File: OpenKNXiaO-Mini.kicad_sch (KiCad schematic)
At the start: 8 parts, among them J1 Conn_KNX, J5 Conn_01x05, J7 Conn_01x12, SW1 Prog BTN, U1 Seeeduino XIAO

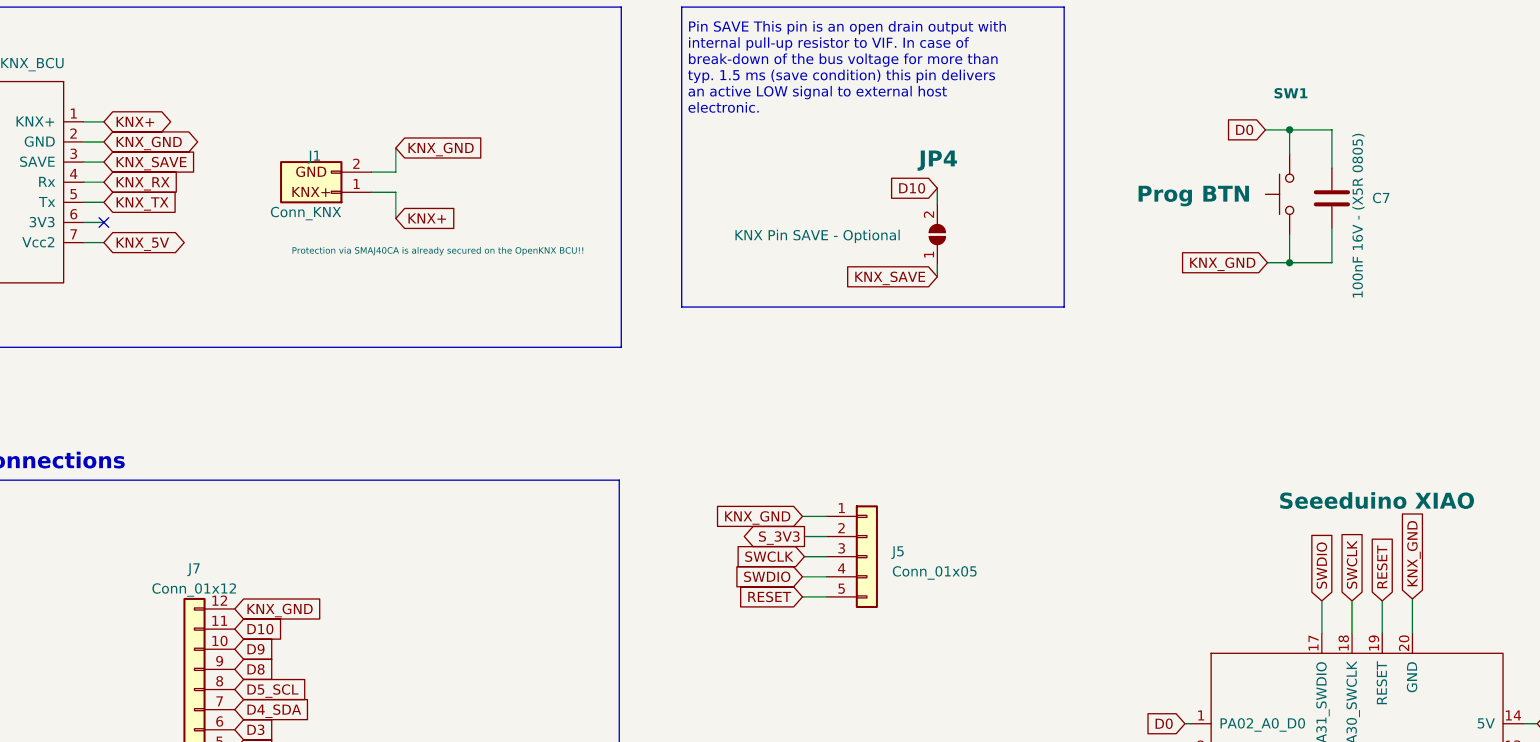
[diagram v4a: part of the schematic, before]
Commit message: Pre-Final
ToDo - Move Save <--> D10 bridge to a reachable place on the pcb
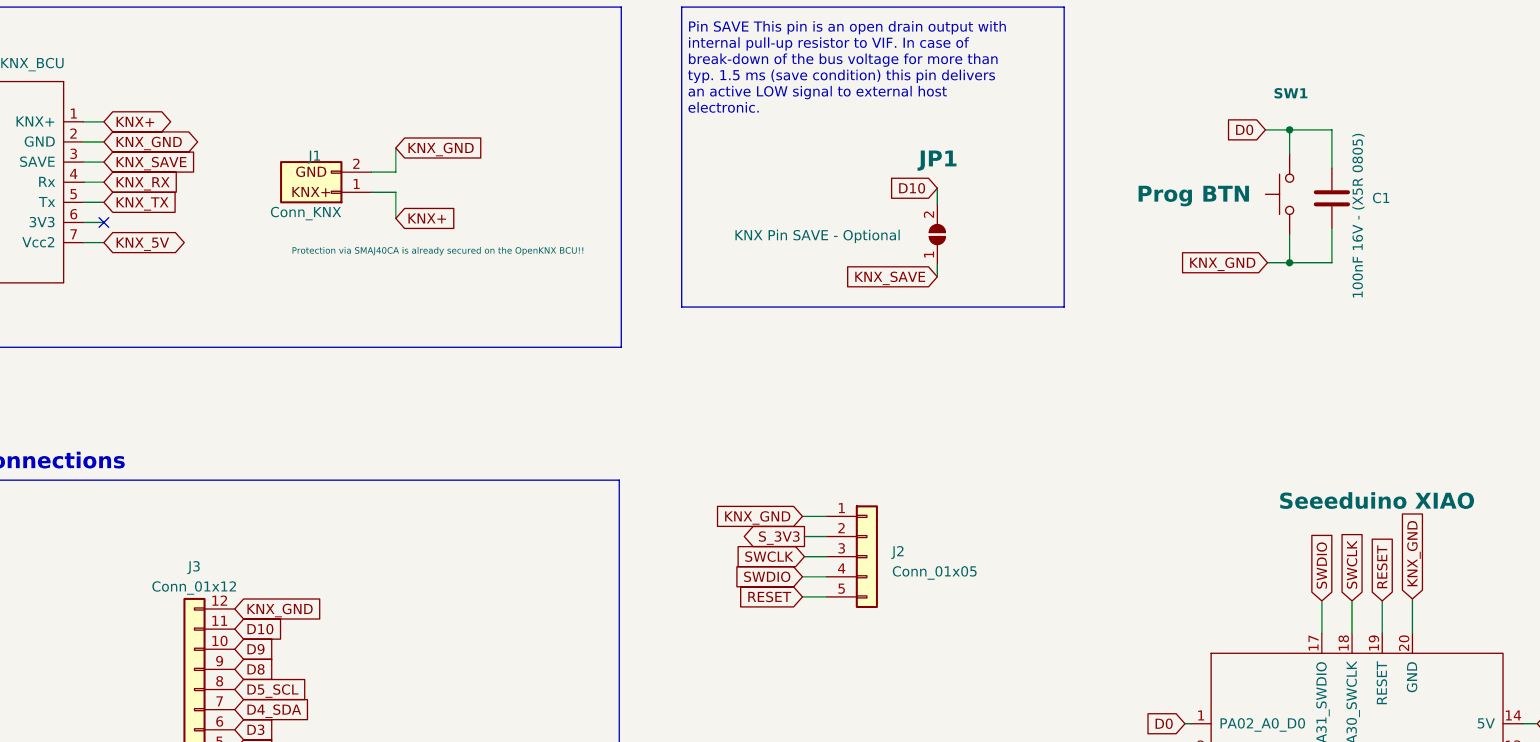
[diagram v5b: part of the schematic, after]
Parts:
- J2: renamed from J5; footprint Connector_JST:JST_SHL_SM05B-SHLS-TF_1x05-1MP_P1.00mm_Horizontal -> Connector_PinHeader_1.00mm:PinHeader_1x05_P1.00mm_Vertical
- renumbered C7 to C1, J7 to J3, JP4 to JP1
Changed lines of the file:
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@@
   (symbol (lib_id "KNeoPix.symbols:SolderJumper_2_Open") (at 142.494 52.07 90) (unit 1)
     (in_bom yes) (on_board yes) (dnp no)
-    (property "Reference" "JP4" (at 142.621 42.545 90)
+    (property "Reference" "JP1" (at 142.621 42.545 90)
       (effects (font (size 2 2) bold))
     )
@@
       (project "OpenKNXiaO-Mini"
         (path "/e63e39d7-6ac0-4ffd-8aa3-1841a4541b55"
-          (reference "JP4") (unit 1)
+          (reference "JP1") (unit 1)
         )
       )
@@
   (symbol (lib_id "Connector_Generic:Conn_01x12") (at 48.768 114.554 180) (unit 1)
     (in_bom yes) (on_board yes) (dnp no) (fields_autoplaced)
-    (property "Reference" "J7" (at 48.768 94.234 0)
+    (property "Reference" "J3" (at 48.768 93.98 0)
       (effects (font (size 1.27 1.27)))
     )
-    (property "Value" "Conn_01x12" (at 48.768 96.774 0)
+    (property "Value" "Conn_01x12" (at 48.768 96.52 0)
       (effects (font (size 1.27 1.27)))
     )
@@
       (project "OpenKNXiaO-Mini"
         (path "/e63e39d7-6ac0-4ffd-8aa3-1841a4541b55"
-          (reference "J7") (unit 1)
+          (reference "J3") (unit 1)
         )
       )
@@
   (symbol (lib_id "KNeoPix.symbols:Conn_01x05") (at 133.604 92.71 0) (unit 1)
     (in_bom yes) (on_board yes) (dnp no) (fields_autoplaced)
-    (property "Reference" "J5" (at 136.779 92.075 0)
+    (property "Reference" "J2" (at 136.779 92.075 0)
       (effects (font (size 1.27 1.27)) (justify left))
     )
@@
       (effects (font (size 1.27 1.27)) (justify left))
     )
-    (property "Footprint" "Connector_JST:JST_SHL_SM05B-SHLS-TF_1x05-1MP_P1.00mm_Horizontal" (at 133.604 92.71 0)
+    (property "Footprint" "Connector_PinHeader_1.00mm:PinHeader_1x05_P1.00mm_Vertical" (at 133.604 92.71 0)
       (effects (font (size 1.27 1.27)) hide)
     )
@@
       (project "OpenKNXiaO-Mini"
         (path "/e63e39d7-6ac0-4ffd-8aa3-1841a4541b55"
-          (reference "J5") (unit 1)
+          (reference "J2") (unit 1)
         )
       )
@@
   (symbol (lib_id "KNeoPix.symbols:C") (at 192.278 47.498 0) (unit 1)
     (in_bom yes) (on_board yes) (dnp no)
-    (property "Reference" "C7" (at 197.358 47.498 0)
+    (property "Reference" "C1" (at 197.358 47.498 0)
       (effects (font (size 1.27 1.27)) (justify left))
     )
@@
       (project "OpenKNXiaO-Mini"
         (path "/e63e39d7-6ac0-4ffd-8aa3-1841a4541b55"
-          (reference "C7") (unit 1)
-        )
-      )
+          (reference "C1") (unit 1)
+        )
+      )

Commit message: Fixed Logo & Version rendering and enabled knx bcu description on back site
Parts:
- J1: SMAJ40 Protection via SMAJ40CA is already secured on the OpenKNX B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 -> Info: Protection via SMAJ40CA is already secured on the Ope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
- J3: value Conn_01x12 -> JST SHL SM12B SHLS TF 1x12-1MP P1.00mm Horizontal
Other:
- note added: "1x KNX-Connector KNX/EIB connector"
- note added: "2x KNX-Connector Pins: WAGO 243-131"
- note added: "I/O Connections"
- note added: "KNX Connection"
- note added: "KNX Prog Botton"
- note added: "KNX SAVE Pin"
- note added: "OpenKNX BCU Connector. Only VCC2 5V is used. The 3V3 in this schematic will not be used. XIAO is powered with 5V supply via 5V-PIN. The XIAO built-in DC-DC converter circuit is able to change 5V voltage into 3.3V."
- note added: "OpenKNX Debug"
- note added: "OpenKNX NanoBCU"
- note added: "Pin SAVE This pin is an open drain output with internal pull-up resistor to VIF. In case of break-down of the bus voltage for more than typ. 1.5 ms (save condition) this pin delivers an active LOW signal to external host electronic. Bridge: Optional. Only valid, when used by Software."
- note added: "Prog Button Pin: D0"
- note removed: "Connections"
- note removed: "KNX Connection and Isolator"
- note removed: "KNX Save"
- note removed: "Pin SAVE This pin is an open drain output with internal pull-up resistor to VIF. In case of break-down of the bus voltage for more than typ. 1.5 ms (save condition) this pin delivers an active LOW signal to external host electronic."
- note removed: "TODO for V1.4 - New Variante: - Reduce to RM1.00 CConnector JST:JST_SH_BM0 P1.00mm - Replace the 2.54 Terminal with JST! - Make is Smaler. No V-External Support! Only KNX! - Add power LED (Bus POWER) ?"
- note removed: "https://wiki.seeedstudio.com/Seeeduino-XIAO/"
- note removed: "https://wiki.seeedstudio.com/XIAO-RP2040/"
- moved on the sheet: C1, GN1, J1, J2, J3, JP1, SW1, U1

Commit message: Changed Title and Date
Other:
- title: KNEoPix -> KNXiao Mini
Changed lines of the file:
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@@
   (paper "A3")
   (title_block
-    (title "KNEoPix")
-    (date "2023-02-12")
-    (rev "1.3")
+    (title "KNXiao Mini")
+    (date "2023-04-28")
+    (rev "1.0")
     (company "OpenKNX")
     (comment 2 "URL: https://github.com/OpenKNX")
